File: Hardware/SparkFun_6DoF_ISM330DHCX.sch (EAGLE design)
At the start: 31 parts, among them J1 QWIIC_RIGHT_ANGLE, J2 QWIIC_RIGHT_ANGLE, U1 ISM330DHCX

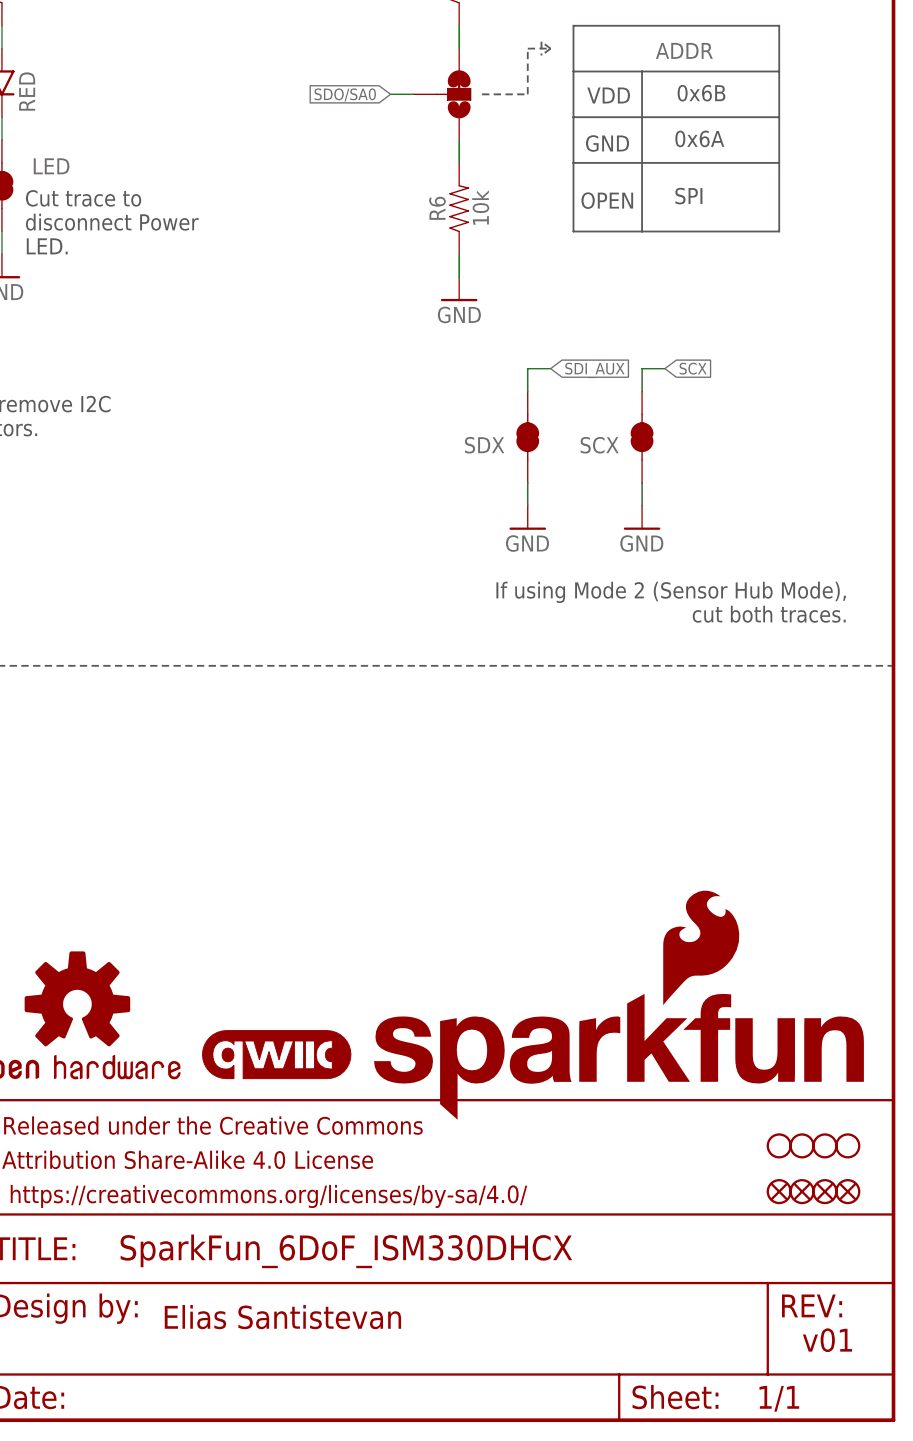
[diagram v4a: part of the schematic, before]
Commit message: Adds labels, fixes wonky box in schematic
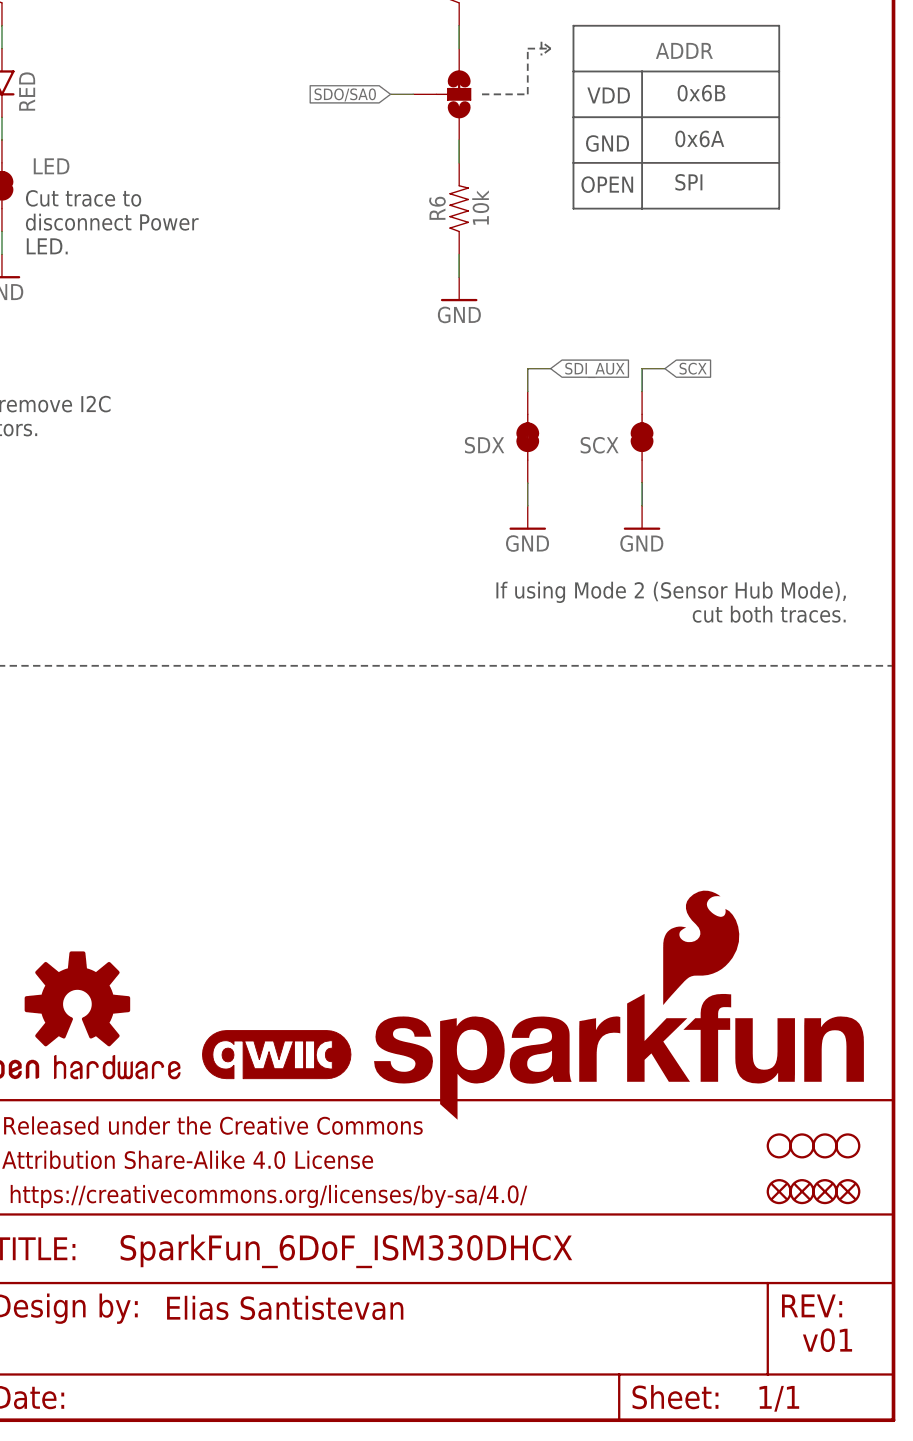
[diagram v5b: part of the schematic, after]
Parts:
- FRAME1: DESIGNER Marshall Taylor -> Elias Santistevan
- LOGO2: value OSHW-LOGOS -> OSHW-LOGOMINI; device SparkFun-Aesthetics:OSHW-LOGOS -> SparkFun-Aesthetics:OSHW-LOGOMINI
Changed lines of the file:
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@@
 <parts>
 <part name="FRAME1" library="SparkFun-Aesthetics" deviceset="FRAME-LETTER" device="">
-<attribute name="DESIGNER" value="Marshall Taylor"/>
+<attribute name="DESIGNER" value="Elias Santistevan"/>
 </part>
 <part name="GND4" library="SparkFun-PowerSymbols" deviceset="GND" device=""/>
@@
 <part name="C4" library="SparkFun-Capacitors" deviceset="0.1UF" device="-0603-25V-(+80/-20%)" value="0.1uF"/>
 <part name="GND10" library="SparkFun-PowerSymbols" deviceset="GND" device=""/>
-<part name="LOGO2" library="SparkFun-Aesthetics" deviceset="OSHW-LOGO" device="S"/>
+<part name="LOGO2" library="SparkFun-Aesthetics" deviceset="OSHW-LOGO" device="MINI" value="OSHW-LOGOMINI"/>
 <part name="STANDOFF1" library="SparkFun-Hardware" deviceset="STAND-OFF" device="TIGHT"/>
 <part name="STANDOFF2" library="SparkFun-Hardware" deviceset="STAND-OFF" device="TIGHT"/>
@@
 <wire x1="213.36" y1="149.86" x2="213.36" y2="144.78" width="0.2032" layer="97"/>
 <wire x1="213.36" y1="144.78" x2="213.36" y2="139.7" width="0.2032" layer="97"/>
-<wire x1="213.36" y1="139.7" x2="213.36" y2="132.08" width="0.2032" layer="97"/>
-<wire x1="213.36" y1="132.08" x2="220.98" y2="132.08" width="0.2032" layer="97"/>
-<wire x1="220.98" y1="132.08" x2="236.22" y2="132.08" width="0.2032" layer="97"/>
-<wire x1="236.22" y1="132.08" x2="236.22" y2="139.7" width="0.2032" layer="97"/>
+<wire x1="213.36" y1="139.7" x2="213.36" y2="134.62" width="0.2032" layer="97"/>
+<wire x1="213.36" y1="134.62" x2="220.98" y2="134.62" width="0.2032" layer="97"/>
+<wire x1="220.98" y1="134.62" x2="236.22" y2="134.62" width="0.2032" layer="97"/>
+<wire x1="236.22" y1="134.62" x2="236.22" y2="139.7" width="0.2032" layer="97"/>
 <wire x1="236.22" y1="139.7" x2="236.22" y2="144.78" width="0.2032" layer="97"/>
 <wire x1="236.22" y1="144.78" x2="236.22" y2="149.86" width="0.2032" layer="97"/>
@@
 <wire x1="220.98" y1="149.86" x2="220.98" y2="144.78" width="0.2032" layer="97"/>
 <wire x1="220.98" y1="144.78" x2="220.98" y2="139.7" width="0.2032" layer="97"/>
-<wire x1="220.98" y1="139.7" x2="220.98" y2="132.08" width="0.2032" layer="97"/>
+<wire x1="220.98" y1="139.7" x2="220.98" y2="134.62" width="0.2032" layer="97"/>
 <wire x1="220.98" y1="144.78" x2="236.22" y2="144.78" width="0.2032" layer="97"/>
 <wire x1="220.98" y1="139.7" x2="236.22" y2="139.7" width="0.2032" layer="97"/>
@@
 <text x="214.884" y="146.304" size="1.778" layer="97" font="vector">VDD</text>
 <text x="214.63" y="140.97" size="1.778" layer="97" font="vector">GND</text>
-<text x="214.122" y="134.62" size="1.778" layer="97" font="vector">OPEN</text>
+<text x="214.122" y="136.398" size="1.778" layer="97" font="vector">OPEN</text>
 <text x="224.79" y="146.558" size="1.778" layer="97" font="vector">0x6B</text>
 <text x="224.536" y="141.478" size="1.778" layer="97" font="vector">0x6A</text>
-<text x="224.536" y="135.128" size="1.778" layer="97" font="vector">SPI</text>
+<text x="224.536" y="136.652" size="1.778" layer="97" font="vector">SPI</text>
 <wire x1="203.2" y1="147.32" x2="208.28" y2="147.32" width="0.2032" layer="97" style="dashdot"/>
 <wire x1="208.28" y1="147.32" x2="208.28" y2="152.4" width="0.2032" layer="97" style="dashdot"/>
@@
 <wire x1="209.804" y1="153.162" x2="209.804" y2="151.638" width="0.2032" layer="97" style="dashdot"/>
 <wire x1="210.82" y1="152.4" x2="209.804" y2="151.638" width="0.2032" layer="97" style="dashdot"/>
-<text x="167.64" y="10.16" size="2.54" layer="94" font="vector">Elias Santistevan</text>
+<text x="167.894" y="11.176" size="2.54" layer="94" font="vector">Elias Santistevan</text>
 </plain>
 <instances>
-<instance part="FRAME1" gate="G$1" x="0" y="0" smashed="yes"/>
+<instance part="FRAME1" gate="G$1" x="0" y="0" smashed="yes">
+<attribute name="DESIGNER" x="0" y="0" size="2.54" layer="96" font="vector" display="off"/>
+</instance>
 <instance part="FRAME1" gate="V" x="147.32" y="0" smashed="yes">
 <attribute name="LAST_DATE_TIME" x="160.02" y="1.27" size="2.54" layer="94" font="vector"/>
